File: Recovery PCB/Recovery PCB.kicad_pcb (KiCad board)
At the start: 2 copper layers, 98.7 x 74.9 mm, 93 parts, among them J1 Conn_01x04_Male, J2 MCU Programming Socket, J3 Conn_01x02, J4 Screw_Terminal_01x02, J5 Screw_Terminal_01x02, J6 MEM2075-00-140-01-A, J7 Conn_01x02_Male, J8 CON-SMA-EDGE-S, J9 CON-SMA-EDGE-S, K1 SANYOU_SRD_Form_C, K2 SANYOU_SRD_Form_C, Q1 BSS138, SW1 SW_Push, SW2 SW_SPDT, U1 ATSAMD21G18A-AUT, U2 MIC5528-3.3YMT-TR, U3 MS5607-02BA, U4 ADXL377, U5 TLP291-4(TP,E), U6 BNO055, U7 RFM95W-915S2, U8 CAM-M8, Y1 32.768kHz, Y2 32.768k

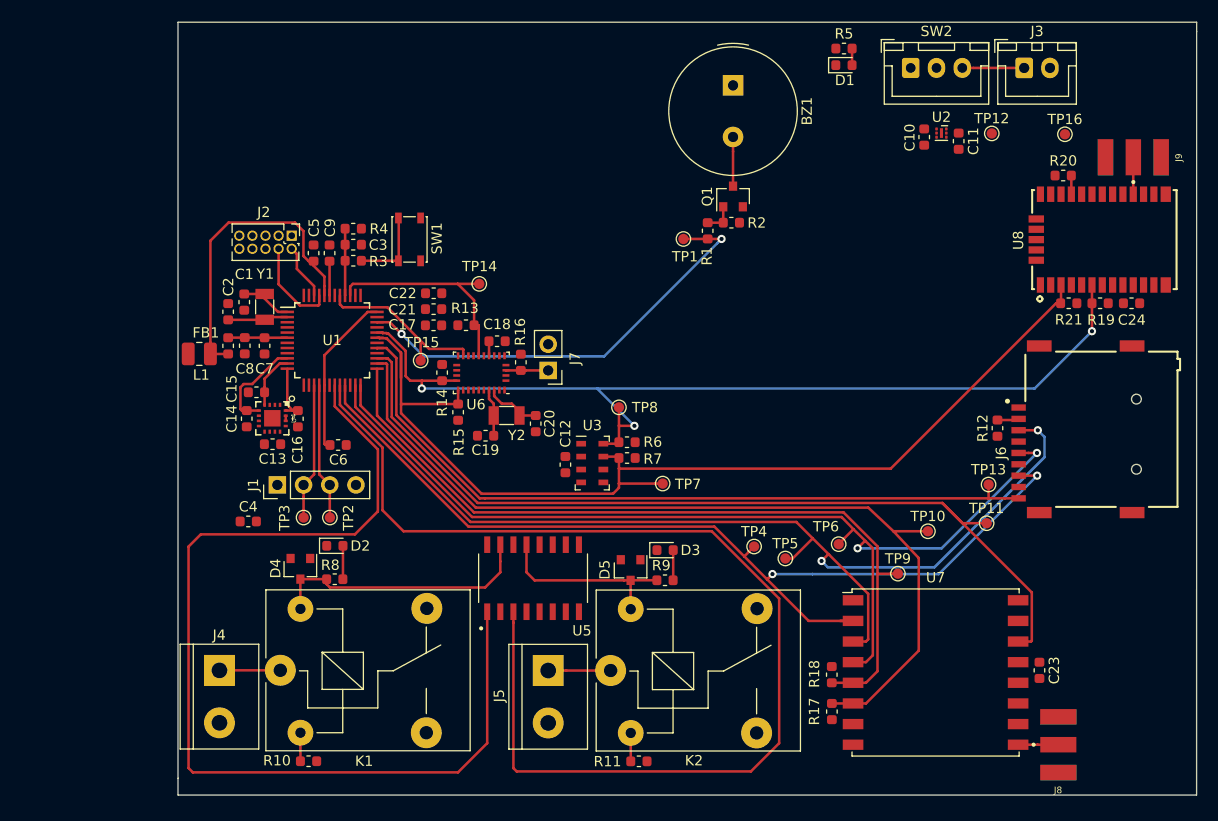
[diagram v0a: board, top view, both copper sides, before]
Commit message: Finished Rev 2 of the Recovery PCB. Optimized trace lengths and relays.
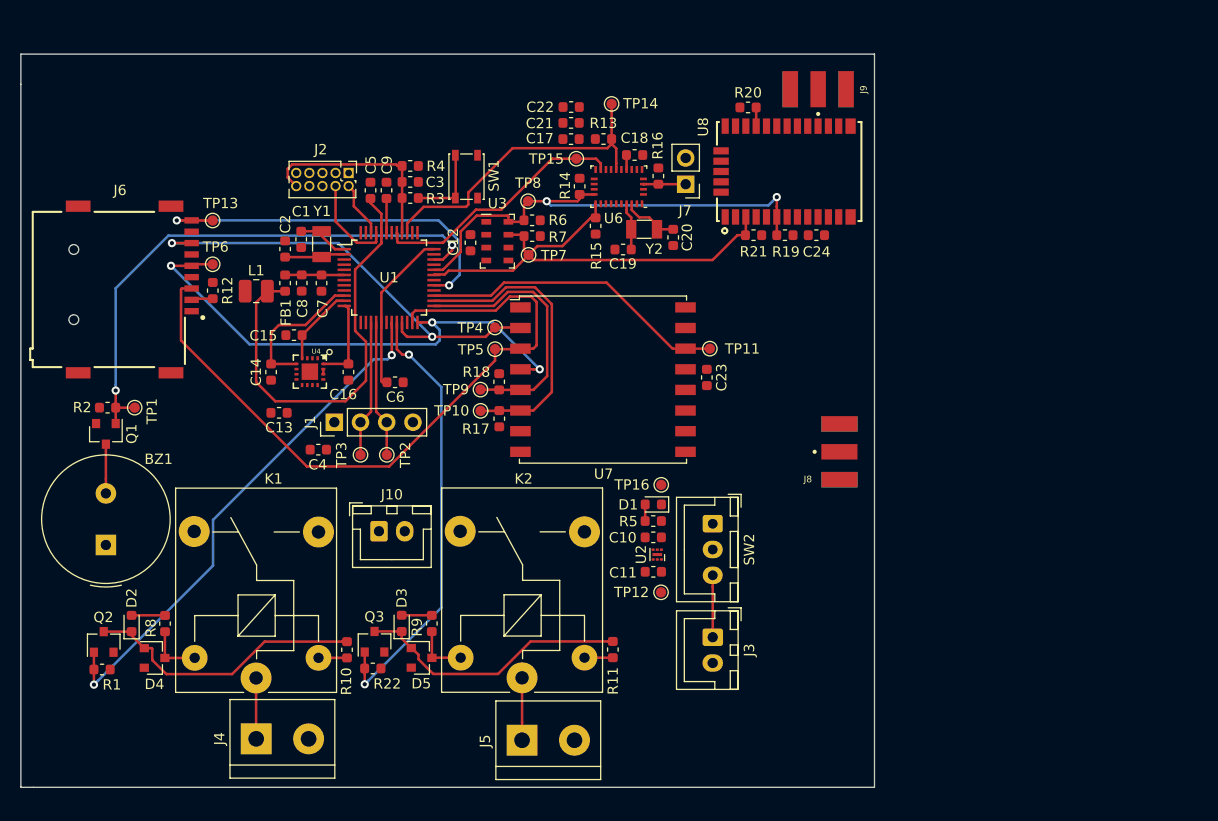
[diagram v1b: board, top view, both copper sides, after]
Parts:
- removed U5: TLP291-4(TP,E), Parts:SOIC127P700X229-16N
- added J10: Conn_01x02_Male, Connector_JST:JST_XH_B2B-XH-A_1x02_P2.50mm_Vertical, F.Cu at (126.8, 99.4)
- added Q2: BSS138, Package_TO_SOT_SMD:SOT-23, F.Cu at (100.1, 110.1)
- added Q3: BSS138, Package_TO_SOT_SMD:SOT-23, F.Cu at (126.3, 110.1)
- added R22: 1M, Resistor_SMD:R_0603_1608Metric, F.Cu at (126.2, 112.7)
- R1: value 1k -> 1M
- moved J6 104.0 mm to (97.2, 75.5), turned to 270 degrees
- moved TP13 79.4 mm to (110.6, 69.3), turned to 180 degrees
- moved R12 77.2 mm to (110.7, 76.1), turned to 270 degrees
- moved BZ1 75.4 mm to (100.3, 100.7), turned to 90 degrees
- moved R1 72.5 mm to (99.9, 112.8), turned to 0 degrees
- moved TP6 66.5 mm to (110.6, 73.5), turned to 180 degrees
- moved Q1 65.0 mm to (100.3, 90.0), turned to 270 degrees
- moved R2 63.1 mm to (100.5, 87.4), turned to 180 degrees
- moved J3 62.9 mm to (159.1, 109.7), turned to 270 degrees
- moved TP1 55.6 mm to (103.1, 87.4), turned to 180 degrees
- moved TP12 54.8 mm to (154.1, 105.3), turned to 270 degrees
- moved TP16 51.8 mm to (154.1, 94.9), turned to 270 degrees
- moved C11 51.2 mm to (153.4, 103.3), turned to 180 degrees
- moved R5 49.4 mm to (153.3, 98.4), turned to 180 degrees
- moved U2 49.3 mm to (153.7, 101.7), turned to 270 degrees
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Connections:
- D2 pad 1: GND -> Net-(D2-Pad1)
- D3 pad 1: GND -> Net-(D3-Pad1)
- D4 pad 1: Net-(D4-Pad1) -> +3V3
- D4 pad 2: GND -> Net-(D2-Pad1)
- D5 pad 1: Net-(D5-Pad1) -> +3V3
- D5 pad 2: GND -> Net-(D3-Pad1)
- J4 pad 2: GND -> GNDPWR
- J5 pad 2: GND -> GNDPWR
- K1 pad 4: Net-(K1-Pad4) -> GNDPWR
- K1 pad 5: Net-(D4-Pad1) -> +3V3
- K2 pad 4: Net-(K2-Pad4) -> GNDPWR
- K2 pad 5: Net-(D5-Pad1) -> +3V3
- Q1 pad 1: Net-(Q1-Pad1) -> /BUZZER
- R1 pad 1: Net-(Q1-Pad1) -> /IN1
- R1 pad 2: /BUZZER -> GND
- R10 pad 2: GND -> Net-(D2-Pad1)
- R11 pad 2: GND -> Net-(D3-Pad1)
- R2 pad 1: Net-(Q1-Pad1) -> /BUZZER
- R8 pad 1: Net-(D4-Pad1) -> +3V3
- R9 pad 1: Net-(D5-Pad1) -> +3V3
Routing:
- net /IN2: track 112.0 -> 43.4 mm, vias 0 -> 2
- net /RADIO_RESET: track 86.3 -> 28.8 mm
- net /RADIO_IO: track 87.1 -> 29.9 mm
- net /SDA: track 102.7 -> 46.9 mm
- net /RADIO_CS: track 77.3 -> 25.9 mm
- net /MISO: track 94.5 -> 43.9 mm
- net /IN1: track 98.2 -> 51.0 mm, vias 0 -> 2
- net /SCL: track 95.1 -> 48.1 mm, vias 3 -> 2
- net /CLK: track 96.0 -> 51.1 mm, vias 2 -> 3
- net /SD_CS: track 72.9 -> 37.9 mm, vias 0 -> 2
- net /MOSI: track 100.7 -> 69.1 mm, vias 2 -> 0
- net Net-(D2-Pad1): track 0.00 -> 27.5 mm
- net Net-(D3-Pad1): track 0.00 -> 26.8 mm
- net Net-(D4-Pad1): track 26.2 -> 0.00 mm
- net Net-(D5-Pad1): track 18.4 -> 0.00 mm
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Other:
- board size 98.7 x 74.9 mm -> 82.7 x 71.1 mm

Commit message: Recovery PCB: Redraw schematics
Redrew Recover PCB schematics to be more easily readable and fixed board
outline, adding netclasses to ease trace placement.
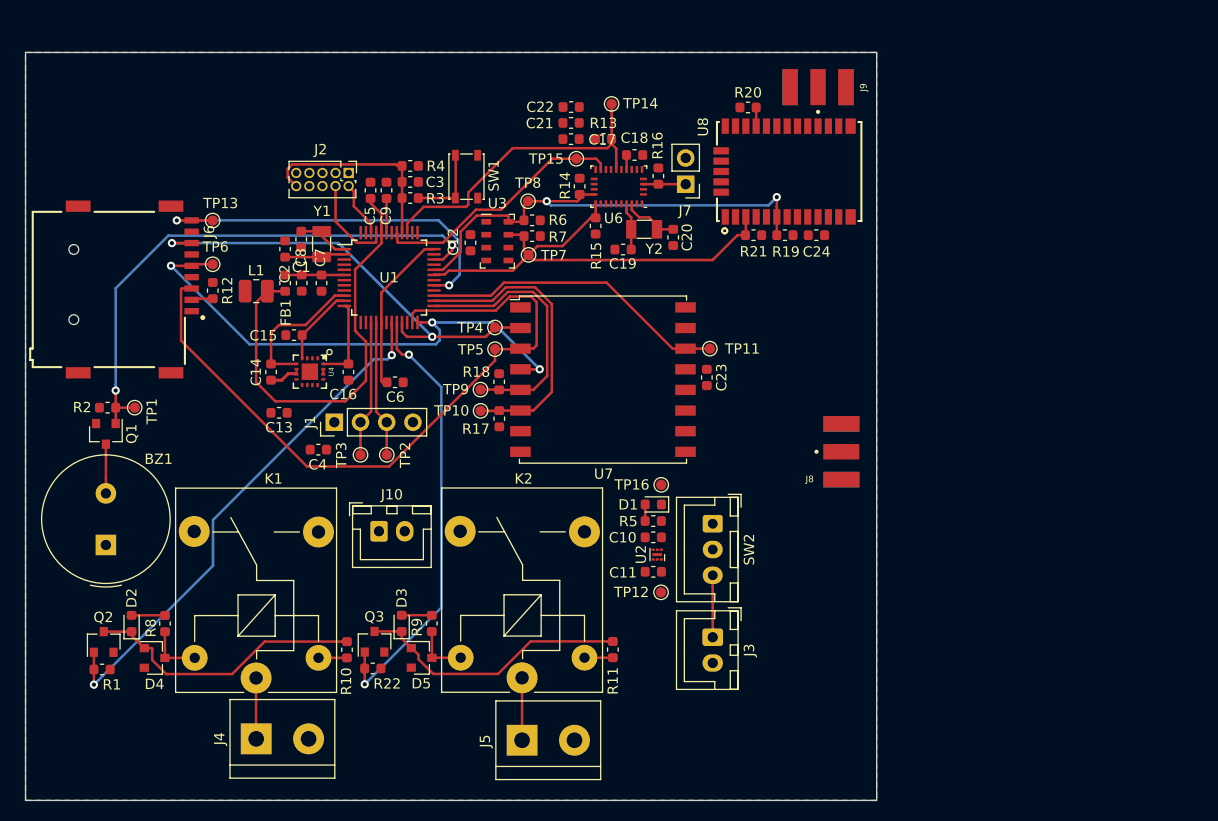
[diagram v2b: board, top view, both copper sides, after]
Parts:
- FB1: value Ferrite_Bead_Small -> Ferrite
- J10: value Conn_01x02_Male -> 9V_INPUT
- J7: value Conn_01x02_Male -> BLD
- J8: value CON-SMA-EDGE-S -> SMA_LORA
- J9: value CON-SMA-EDGE-S -> SMA_GPS
- moved J9 0.20 mm to (169.3, 56.4)
- moved J8 0.18 mm to (171.6, 91.7)
- turned C1 to 90 degrees
- turned C17 to 180 degrees
- turned C2 to 270 degrees
- turned C5 to 270 degrees
- turned C7 to 270 degrees
- turned C8 to 270 degrees
- turned C9 to 90 degrees
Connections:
- net Net-(J8-Pad1) renamed /radio-915-lora/LoRa_RF
- net Net-(J9-Pad1) renamed /gps-module/GPS_RF
- C1 pad 1: Net-(C1-Pad1) -> GND
- C1 pad 2: GND -> Net-(C1-Pad2)
- C17 pad 1: GND -> +3V3
- C17 pad 2: +3V3 -> GND
- C2 pad 1: Net-(C2-Pad1) -> GND
- C2 pad 2: GND -> Net-(C2-Pad2)
- C24 pad 1: GND -> +3V3
- C24 pad 2: +3V3 -> GND
- C4 pad 1: +3V3 -> Net-(C4-Pad1)
- C5 pad 1: Net-(C5-Pad1) -> GND
- C5 pad 2: GND -> Net-(C4-Pad1)
- C6 pad 1: Net-(C6-Pad1) -> Net-(C4-Pad1)
- C7 pad 1: GND -> Net-(C7-Pad1)
- C7 pad 2: Net-(C7-Pad2) -> GND
- C8 pad 1: GND -> Net-(C7-Pad1)
- C8 pad 2: Net-(C7-Pad2) -> GND
- C9 pad 1: GND -> Net-(C9-Pad1)
- C9 pad 2: Net-(C9-Pad2) -> GND
- FB1 pad 1: Net-(C7-Pad2) -> Net-(C7-Pad1)
- FB1 pad 2: Net-(C5-Pad1) -> Net-(C4-Pad1)
- L1 pad 2: Net-(C5-Pad1) -> Net-(C4-Pad1)
- U1 pad 1: Net-(C1-Pad1) -> Net-(C1-Pad2)
- U1 pad 17: Net-(C6-Pad1) -> Net-(C4-Pad1)
- U1 pad 2: Net-(C2-Pad1) -> Net-(C2-Pad2)
- U1 pad 36: Net-(C6-Pad1) -> Net-(C4-Pad1)
- U1 pad 43: Net-(C9-Pad2) -> Net-(C9-Pad1)
- U1 pad 44: Net-(C5-Pad1) -> Net-(C4-Pad1)
- U1 pad 6: Net-(C7-Pad2) -> Net-(C7-Pad1)
- Y1 pad 1: Net-(C1-Pad1) -> Net-(C1-Pad2)
- Y1 pad 2: Net-(C2-Pad1) -> Net-(C2-Pad2)
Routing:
- net Net-(C4-Pad1): track 0.00 -> 58.8 mm
- net Net-(C5-Pad1): track 42.8 -> 0.00 mm
- net Net-(C6-Pad1): track 16.0 -> 0.00 mm
- net Net-(C2-Pad2): track 0.00 -> 5.84 mm
- net Net-(C2-Pad1): track 5.84 -> 0.00 mm
- net Net-(C7-Pad2): track 5.74 -> 0.00 mm
- net Net-(C7-Pad1): track 0.00 -> 5.74 mm
- net Net-(C1-Pad2): track 0.00 -> 5.15 mm
- net Net-(C1-Pad1): track 5.15 -> 0.00 mm
- net Net-(C9-Pad2): track 3.32 -> 0.00 mm
- net Net-(C9-Pad1): track 0.00 -> 3.32 mm
- net GND: track 0.00 -> 3.29 mm
- added copper zone on In2.Cu, net +3V3
- added copper zone on B.Cu, net GND
- added copper zone on F.Cu, net GND
- added copper zone on In1.Cu, net GND
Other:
- board size 82.7 x 71.1 mm -> 82.5 x 72.5 mm
- copper layers 2 -> 4
- net class Default: via_dia 0.8 -> 0.6; via_drill 0.4 -> 0.35
- net class Local Power added: clearance 0.2, trace_width 0.254, via_dia 0.6, via_drill 0.35
- net class Power added: clearance 0.25, trace_width 0.3048, via_dia 0.8, via_drill 0.4
- net class RF 50 Ohm added: clearance 0.2, trace_width 0.25, via_dia 0.6, via_drill 0.35
- net class Signal added: clearance 0.16, trace_width 0.2032, via_dia 0.6, via_drill 0.35

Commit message: Rev 3 of Recovery PCB. Fixed decoupling caps and finalized power/ground.
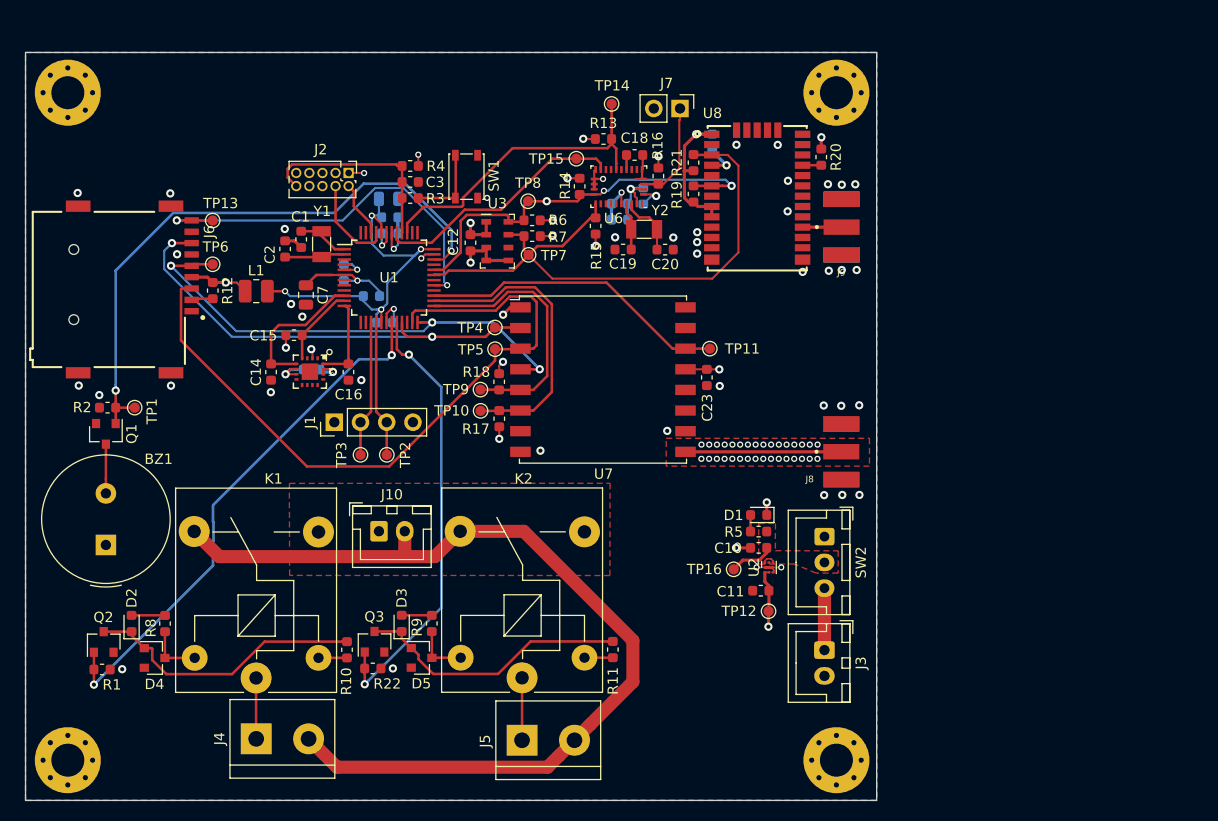
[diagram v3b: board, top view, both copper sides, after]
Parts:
- added REF**: MountingHole_3.2mm_M3_Pad_Via, MountingHole:MountingHole_3.2mm_M3_Pad_Via, F.Cu at (96.6, 121.6)
- added REF**: MountingHole_3.2mm_M3_Pad_Via, MountingHole:MountingHole_3.2mm_M3_Pad_Via, F.Cu at (171.1, 121.6)
- added REF**: MountingHole_3.2mm_M3_Pad_Via, MountingHole:MountingHole_3.2mm_M3_Pad_Via, F.Cu at (171.1, 56.9)
- added REF**: MountingHole_3.2mm_M3_Pad_Via, MountingHole:MountingHole_3.2mm_M3_Pad_Via, F.Cu at (96.6, 56.9)
- C13, C17, C21, C22, C24, C5, C6, C8, C9, FB1: moved to B.Cu
- C4: footprint Capacitor_SMD:C_0603_1608Metric -> Capacitor_SMD:C_0805_2012Metric; moved to B.Cu
- C7: footprint Capacitor_SMD:C_0603_1608Metric -> Capacitor_SMD:C_0805_2012Metric
- moved C4 25.2 mm to (127.7, 67.2)
- moved J9 13.8 mm to (171.6, 69.9), turned to 180 degrees
- moved C24 13.5 mm to (159.1, 61.7), turned to 270 degrees
- moved C22 11.9 mm to (150.1, 69.2)
- moved J3 10.9 mm to (169.9, 110.9)
- moved SW2 10.9 mm to (169.9, 99.9)
- moved U2 10.9 mm to (164.6, 102.9), turned to 90 degrees
- moved TP16 10.8 mm to (161.1, 103.1)
- moved C11 10.6 mm to (163.8, 105.2)
- moved TP12 10.6 mm to (164.5, 107.2)
- moved C10 10.3 mm to (163.6, 101.0)
- moved D1 10.3 mm to (163.6, 97.8)
- moved R5 10.3 mm to (163.6, 99.4)
- moved R19 9.72 mm to (157.2, 66.7), turned to 90 degrees
- moved C21 9.13 mm to (150.1, 67.7)
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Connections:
- U2 pad 1: +BATT -> +3V3
- U2 pad 2: GND -> +3V3
- U2 pad 3: +BATT -> GND
- U2 pad 4: Net-(U2-Pad4) -> +BATT
- U2 pad 5: +3V3 -> Net-(U2-Pad5)
- U2 pad 6: (no net) -> +BATT
- U2 pad 7: (no net) -> GND
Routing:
- net GNDPWR: track 0.00 -> 91.5 mm
- net +3V3: track 11.3 -> 68.0 mm, vias 0 -> 18
- net GND: track 3.29 -> 50.9 mm, vias 0 -> 88
- net Net-(C4-Pad1): track 58.8 -> 36.7 mm, vias 0 -> 4
- net /radio-915-lora/LoRa_RF: track 0.00 -> 15.1 mm
- net /SDA: track 46.9 -> 58.4 mm
- net /SCL: track 48.1 -> 40.2 mm, vias 2 -> 3
- net /BUZZER: track 52.7 -> 58.7 mm
- net Net-(J7-Pad1): track 4.11 -> 9.95 mm
- net +BATT: track 0.00 -> 5.65 mm
- net Net-(C7-Pad1): track 5.74 -> 9.99 mm, vias 0 -> 1
- net /gps-module/GPS_RF: track 0.01 -> 3.79 mm
- net /CLK: track 51.1 -> 48.0 mm
- net /MISO: track 43.9 -> 46.4 mm
- net /SD_CS: track 37.9 -> 39.2 mm
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- added copper zone on F.Cu, net +9V
- added copper zone on F.Cu, net +BATT
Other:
- net class Coplanar Wave Guide 50 Ohm added: clearance 0.2, trace_width 0.325628, via_dia 0.6, via_drill 0.35
- net class Power: clearance 0.25 -> 0.2
- net class RF 50 Ohm: trace_width 0.25 -> 0.319024
- rule trace_min: 0.2 -> 0.13

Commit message: Recovery PCB: Optimize space
Reduced board space by shifting layout a bit.
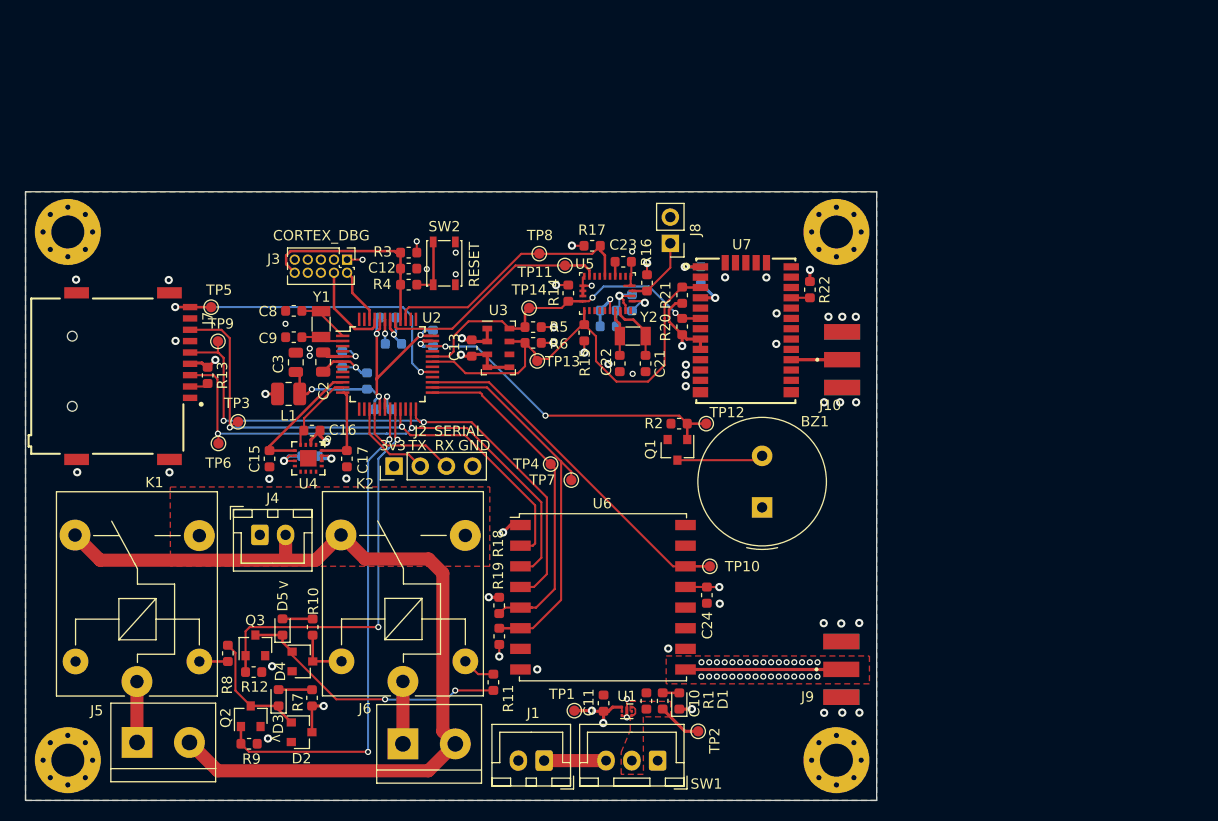
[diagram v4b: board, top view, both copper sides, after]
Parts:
- removed the TP2 at (127.5, 92.0)
- removed the TP3 at (125.0, 92.0)
- added C5: 100n, Capacitor_SMD:C_0603_1608Metric, B.Cu at (132.0, 80.7)
- C3: renamed from C4; moved to F.Cu
- moved BZ1 63.7 mm to (163.9, 97.1)
- moved Q1 55.4 mm to (155.7, 91.5)
- moved R2 55.4 mm to (155.9, 89.0)
- moved TP12 55.4 mm to (158.5, 89.0)
- moved J1 29.2 mm to (142.8, 121.6), turned to 180 degrees
- moved TP6 28.3 mm to (111.2, 90.9)
- moved SW1 27.1 mm to (153.8, 121.6), turned to 180 degrees
- moved TP3 26.5 mm to (113.1, 88.8)
- moved R18 21.7 mm to (138.4, 106.6)
- moved TP1 21.1 mm to (145.7, 116.8), turned to 180 degrees
- moved C24 21.1 mm to (158.5, 105.6)
- moved TP10 21.1 mm to (158.8, 102.8)
- moved U6 21.1 mm to (148.5, 105.8)
- moved J9 21.1 mm to (171.6, 112.8)
- moved R19 21.1 mm to (138.4, 109.6)
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- renumbered C8 to C1, C3 to C12, C12 to C13, C13 to C14, C14 to C15, C15 to C16, C16 to C17, C17 to C18, C21 to C19, C7 to C2, C22 to C20, C19 to C21, C20 to C22, C18 to C23, C23 to C24, C24 to C25, C6 to C4, C5 to C6, C9 to C7, C1 to C8, C2 to C9, D4 to D2, D2 to D3, D5 to D4, D3 to D5, J3 to J1, J9 to J10, J1 to J2, J2 to J3, J10 to J4, J4 to J5, J5 to J6, J6 to J7, J7 to J8, J8 to J9, R5 to R1, R9 to R10, R22 to R12, R12 to R13, R13 to R17, R17 to R19, R19 to R20, R20 to R22, R4 to R3, R3 to R4, R6 to R5, R7 to R6, R8 to R7, R10 to R8, R1 to R9, SW2 to SW1, SW1 to SW2, TP12 to TP1, TP11 to TP10, TP15 to TP11, TP1 to TP12, TP7 to TP13, TP8 to TP14, TP16 to TP2, TP4 to TP3, TP9 to TP4, TP13 to TP5, TP5 to TP6, TP10 to TP7, TP14 to TP8, TP6 to TP9, U2 to U1, U1 to U2, U6 to U5, U7 to U6, U8 to U7
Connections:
- net Net-(J1-Pad2) renamed /UART_TX
- net Net-(J1-Pad3) renamed /UART_RX
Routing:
- net /BUZZER: track 58.7 -> 31.2 mm
- net Net-(D2-Pad2): track 27.5 -> 11.6 mm
- net /MOSI: track 69.1 -> 53.4 mm, vias 0 -> 2
- net /SDA: track 58.4 -> 45.2 mm
- net /RADIO_RESET: track 28.8 -> 38.2 mm
- net /CLK: track 48.0 -> 57.4 mm, vias 3 -> 2
- net /RADIO_CS: track 25.9 -> 34.2 mm
- net /SCL: track 40.2 -> 32.4 mm, vias 3 -> 2
- net /MISO: track 46.4 -> 53.8 mm
- net +3V3: track 68.0 -> 61.4 mm, vias 18 -> 22
- net Net-(C3-Pad1): track 36.7 -> 31.2 mm
- net /SD_CS: track 39.2 -> 33.7 mm
- net /IMU_RESET: track 30.9 -> 25.5 mm
- net GNDPWR: track 91.5 -> 86.8 mm
- net /UART_TX: track 13.3 -> 8.62 mm
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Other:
- board size 82.5 x 72.5 mm -> 82.5 x 59 mm
- board text added: "3v3"
- board text added: "<"
- board text added: ">"
- board text added: "CORTEX_DBG"
- board text added: "GND"
- board text added: "RESET"
- board text added: "RX"
- board text added: "SERIAL"
- board text added: "TX"
